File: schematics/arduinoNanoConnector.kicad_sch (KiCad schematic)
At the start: 5 parts, among them J17 myBus, U16 CD74HCT299E, U17 ArduinoNano, U18 CD74HCT299E, U19 CD74HCT299E

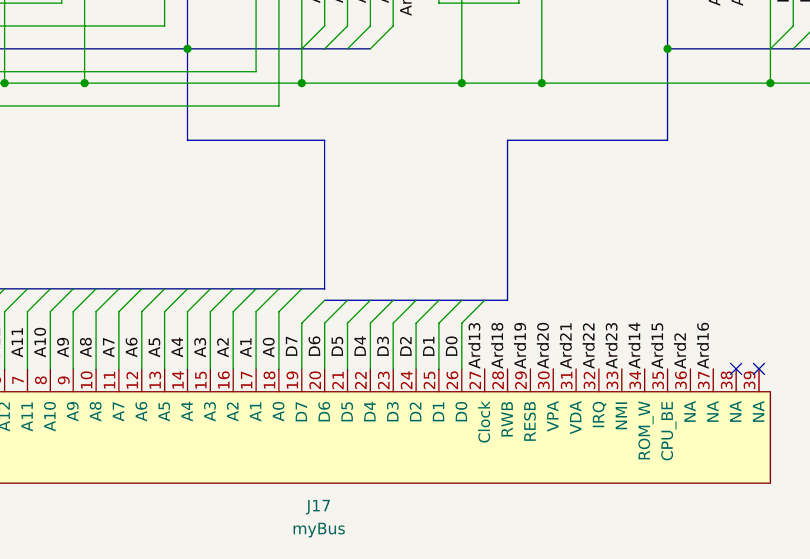
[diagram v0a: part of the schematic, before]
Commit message: Fix errors in schematics
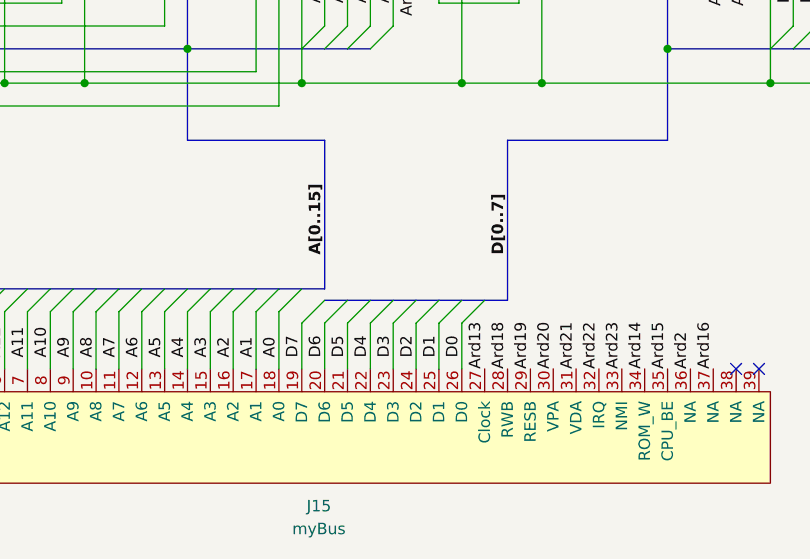
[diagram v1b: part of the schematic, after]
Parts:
- renumbered J17 to J15
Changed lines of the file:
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@@
+		)
+	)
+	(label "A[0..15]"
+		(at 110.49 152.4 90)
+		(fields_autoplaced yes)
+		(effects
+			(font
+				(size 1.27 1.27)
+				(bold yes)
+			)
+			(justify left bottom)
 		)
 	)
@@
 			(font
 				(size 1.27 1.27)
+			)
+			(justify left bottom)
+		)
+	)
+	(label "D[0..7]"
+		(at 130.81 152.4 90)
+		(fields_autoplaced yes)
+		(effects
+			(font
+				(size 1.27 1.27)
+				(bold yes)
 			)
 			(justify left bottom)
@@
 		(on_board yes)
 		(dnp no)
-		(property "Reference" "#PWR088"
+		(property "Reference" "#PWR080"
 			(at 138.43 35.56 0)
 			(effects
@@
 			(project "markus"
 				(path "/03a78ca6-eaff-4f05-be7b-36cd15f8b56d/9b76e599-4a5e-440d-8b73-318ab6b67914"
-					(reference "#PWR088")
+					(reference "#PWR080")
 					(unit 1)
 				)
@@
 		(on_board yes)
 		(dnp no)
-		(property "Reference" "#PWR085"
+		(property "Reference" "#PWR077"
 			(at 46.99 88.9 0)
 			(effects
@@
 			(project "markus"
 				(path "/03a78ca6-eaff-4f05-be7b-36cd15f8b56d/9b76e599-4a5e-440d-8b73-318ab6b67914"
-					(reference "#PWR085")
+					(reference "#PWR077")
 					(unit 1)
 				)
@@
 		(on_board yes)
 		(dnp no)
-		(property "Reference" "#PWR086"
+		(property "Reference" "#PWR078"
 			(at 54.61 171.45 0)
 			(effects
@@
 			(project "markus"
 				(path "/03a78ca6-eaff-4f05-be7b-36cd15f8b56d/9b76e599-4a5e-440d-8b73-318ab6b67914"
-					(reference "#PWR086")
+					(reference "#PWR078")
 					(unit 1)
 				)
@@
 		(on_board yes)
 		(dnp no)
-		(property "Reference" "#PWR087"
+		(property "Reference" "#PWR079"
 			(at 57.15 162.56 0)
 			(effects
@@
 			(project "markus"
 				(path "/03a78ca6-eaff-4f05-be7b-36cd15f8b56d/9b76e599-4a5e-440d-8b73-318ab6b67914"
-					(reference "#PWR087")
+					(reference "#PWR079")
 					(unit 1)
 				)
@@
 		(on_board yes)
 		(dnp no)
-		(property "Reference" "#PWR084"
+		(property "Reference" "#PWR076"
 			(at 45.72 143.51 0)
 			(effects
@@
 			(project "markus"
 				(path "/03a78ca6-eaff-4f05-be7b-36cd15f8b56d/9b76e599-4a5e-440d-8b73-318ab6b67914"
-					(reference "#PWR084")
+					(reference "#PWR076")
 					(unit 1)
 				)
@@
 		(dnp no)
 		(fields_autoplaced yes)
-		(property "Reference" "J17"
+		(property "Reference" "J15"
 			(at 109.855 180.34 0)
 			(effects
@@
 			(project ""
 				(path "/03a78ca6-eaff-4f05-be7b-36cd15f8b56d/9b76e599-4a5e-440d-8b73-318ab6b67914"
-					(reference "J17")
+					(reference "J15")
 					(unit 1)
 				)
@@
 		(on_board yes)
 		(dnp no)
-		(property "Reference" "#PWR089"
+		(property "Reference" "#PWR081"
 			(at 138.43 67.31 0)
 			(effects
@@
 			(project "markus"
 				(path "/03a78ca6-eaff-4f05-be7b-36cd15f8b56d/9b76e599-4a5e-440d-8b73-318ab6b67914"
-					(reference "#PWR089")
+					(reference "#PWR081")
 					(unit 1)
 				)

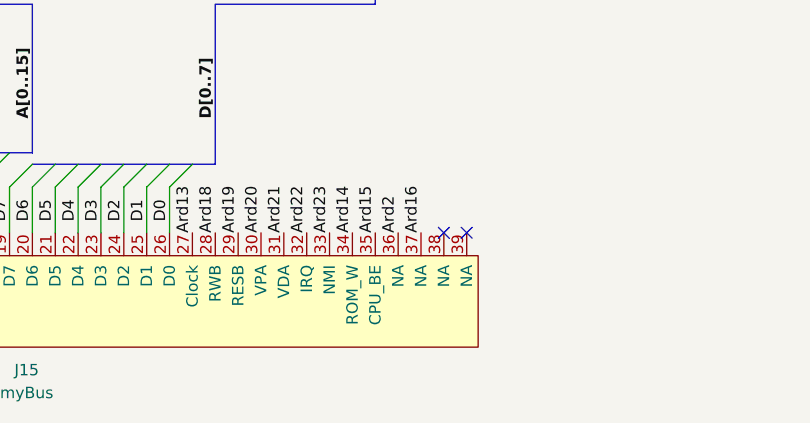
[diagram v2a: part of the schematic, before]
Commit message: Update ROM design
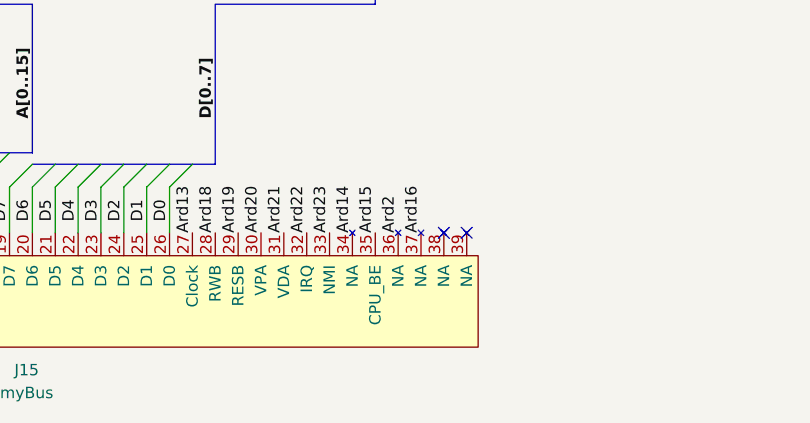
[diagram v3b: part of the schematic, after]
